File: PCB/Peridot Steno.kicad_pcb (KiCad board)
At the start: 2 copper layers, 190.5 x 107.9 mm, 67 parts, among them J1 LED VCC, J2 LED DAT, J3 LED GND, SW1 RESET, SW11 #, SW12 P, SW13 W, SW17 H, SW18 R, SW19 A, SW2 #, SW21 *, SW23 O, SW25 #, SW26 F, SW27 R, SW28 *, SW30 P, SW31 B, SW32 E, SW33 #, SW34 L, SW35 G, SW36 U, SW38 T, SW39 S, SW4 S, SW42 D, SW43 Z, SW8 T, SW9 K, U1 ProMicro

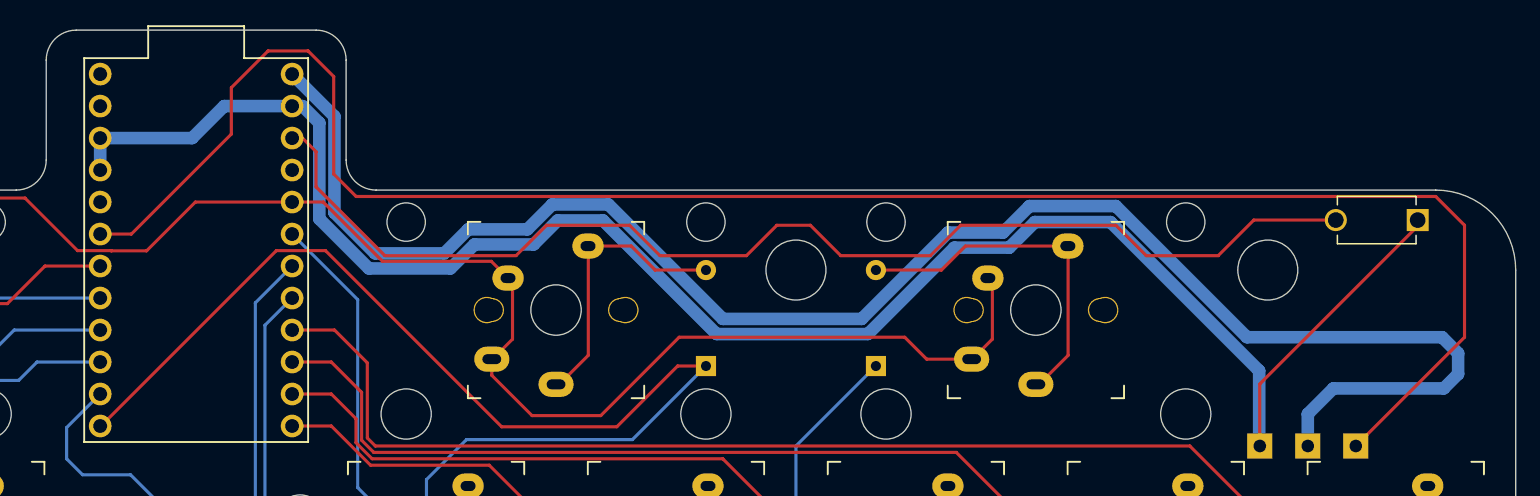
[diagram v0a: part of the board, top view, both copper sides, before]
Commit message: Fixed collision with USB-C connector and removed weird snake like trace
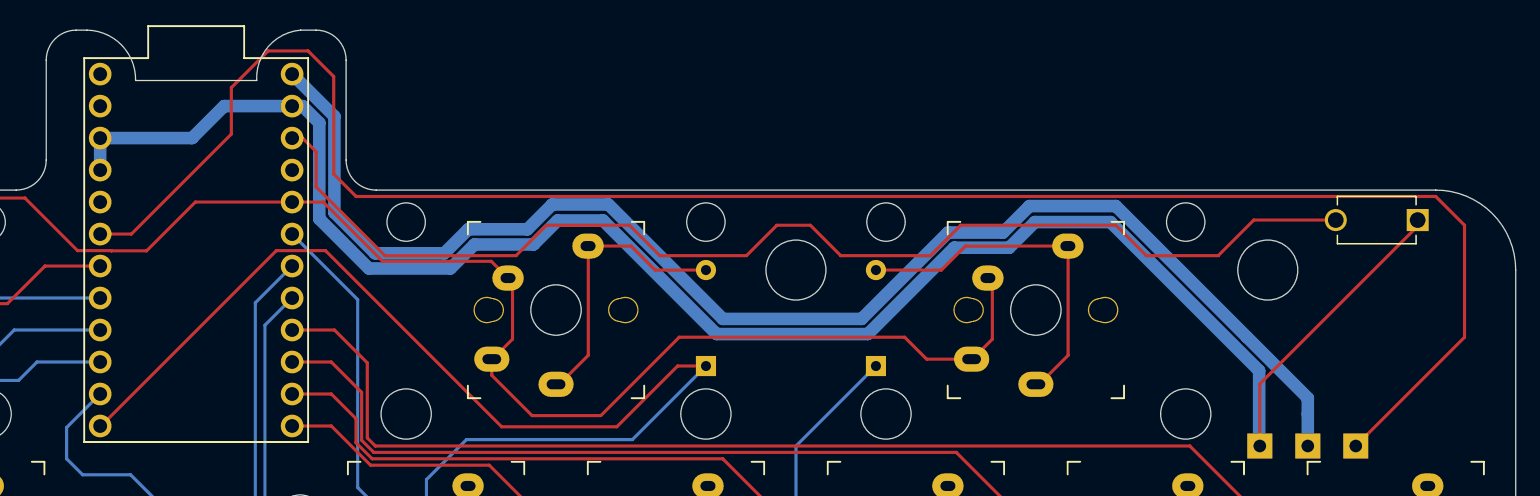
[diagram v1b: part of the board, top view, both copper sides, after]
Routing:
- net +5V: track 134.3 -> 110.2 mm
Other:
- outline, holes or cut-outs redrawn

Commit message: Fixed Trace
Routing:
- net LED_DAT: track 147.9 -> 137.2 mm
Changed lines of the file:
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@@
 	)
 	(segment
-		(start 135.255 41.5925)
+		(start 151.002412 32.7475)
+		(end 146.5765 32.7475)
+		(width 0.25)
+		(layer "F.Cu")
+		(net 40)
+	)
+	(segment
+		(start 153.797 36.83)
+		(end 153.797 35.542088)
+		(width 0.25)
+		(layer "F.Cu")
+		(net 40)
+	)
+	(segment
+		(start 243.586 40.894)
+		(end 241.3 38.608)
+		(width 0.25)
+		(layer "F.Cu")
+		(net 40)
+	)
+	(segment
+		(start 153.797 35.542088)
+		(end 151.002412 32.7475)
+		(width 0.25)
+		(layer "F.Cu")
+		(net 40)
+	)
+	(segment
+		(start 243.586 49.784)
+		(end 243.586 40.894)
+		(width 0.25)
+		(layer "F.Cu")
+		(net 40)
+	)
+	(segment
+		(start 155.575 38.608)
+		(end 153.797 36.83)
+		(width 0.25)
+		(layer "F.Cu")
+		(net 40)
+	)
+	(segment
+		(start 241.3 38.608)
+		(end 155.575 38.608)
+		(width 0.25)
+		(layer "F.Cu")
+		(net 40)
+	)
+	(segment
+		(start 137.7315 41.5925)
+		(end 135.255 41.5925)
+		(width 0.25)
+		(layer "F.Cu")
+		(net 40)
+	)
+	(segment
+		(start 146.5765 32.7475)
 		(end 137.7315 41.5925)
 		(width 0.25)
@@
 	)
 	(segment
-		(start 153.797 29.083)
-		(end 153.797 36.83)
-		(width 0.25)
-		(layer "F.Cu")
-		(net 40)
-	)
-	(segment
-		(start 153.797 36.83)
-		(end 155.575 38.608)
-		(width 0.25)
-		(layer "F.Cu")
-		(net 40)
-	)
-	(segment
-		(start 155.575 38.608)
-		(end 241.3 38.608)
-		(width 0.25)
-		(layer "F.Cu")
-		(net 40)
-	)
-	(segment
-		(start 241.3 38.608)
-		(end 243.586 40.894)
-		(width 0.25)
-		(layer "F.Cu")
-		(net 40)
-	)
-	(segment
-		(start 243.586 40.894)
+		(start 234.95 58.42)
 		(end 243.586 49.784)
 		(width 0.25)
 		(layer "F.Cu")
-		(net 40)
-	)
-	(segment
-		(start 137.7315 41.5925)
-		(end 145.669 33.655)
-		(width 0.25)
-		(layer "F.Cu")
-		(net 40)
-	)
-	(segment
-		(start 243.586 49.784)
-		(end 234.95 58.42)
-		(width 0.25)
-		(layer "F.Cu")
-		(net 40)
-	)
-	(segment
-		(start 145.669 29.972)
-		(end 148.59 27.051)
-		(width 0.25)
-		(layer "F.Cu")
-		(net 40)
-	)
-	(segment
-		(start 151.765 27.051)
-		(end 153.797 29.083)
-		(width 0.25)
-		(layer "F.Cu")
-		(net 40)
-	)
-	(segment
-		(start 148.59 27.051)
-		(end 151.765 27.051)
-		(width 0.25)
-		(layer "F.Cu")
-		(net 40)
-	)
-	(segment
-		(start 145.669 33.655)
-		(end 145.669 29.972)
-		(width 0.25)
-		(layer "F.Cu")
